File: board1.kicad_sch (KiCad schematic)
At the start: 24 parts, among them J1 Conn_01x14_Female, J2 Conn_01x05_Female, J3 Conn_01x14_Female, J4 Conn_01x20_Female, J5 Conn_01x20_Female, J6 XT30 Male Connector, U1 BNO085, U2 Teensy_4.0, U3 Raspberry_PI_Zero_W, U4 D24V50F5

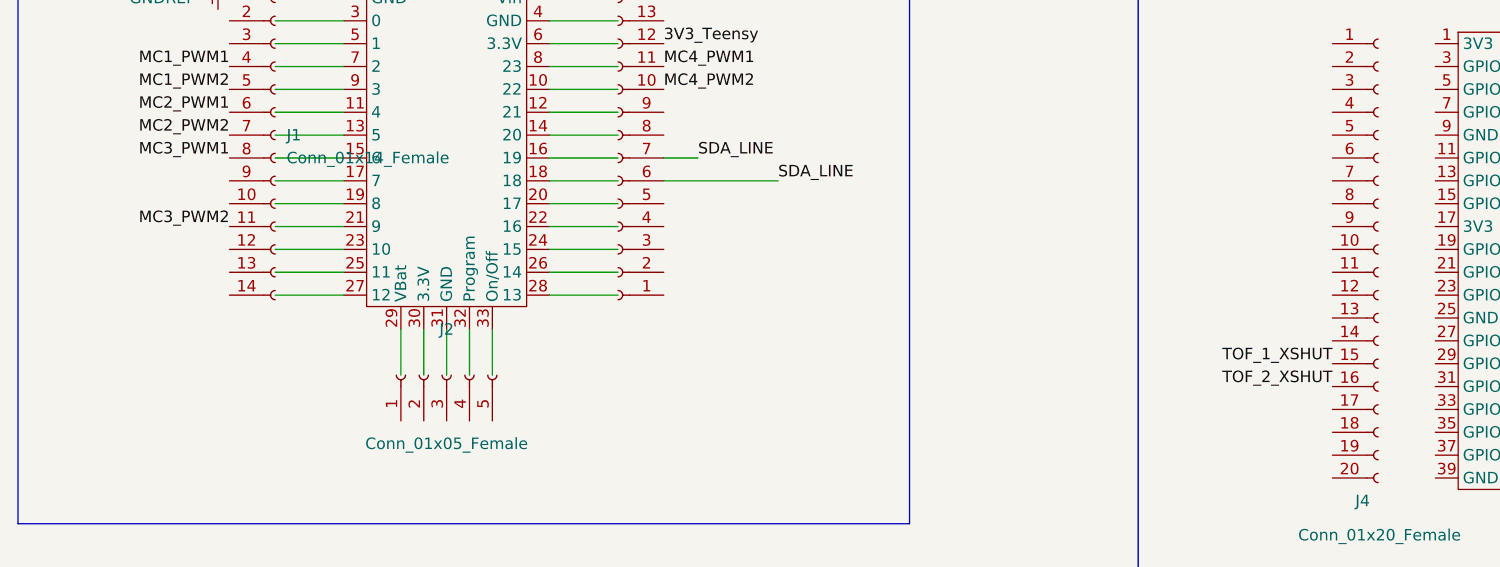
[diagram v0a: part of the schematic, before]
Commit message: Connected RPI to Teensy SPI
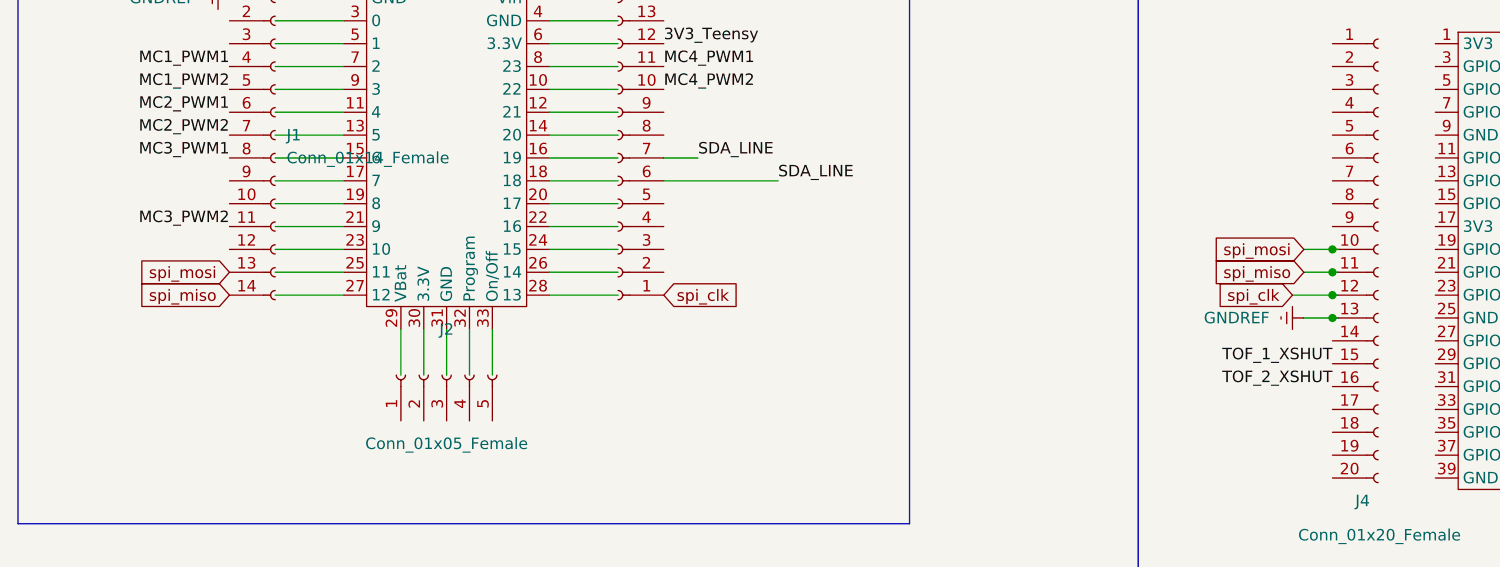
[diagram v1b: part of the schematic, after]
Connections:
- net GNDREF: now also J4.13 (Pin_13)
- net spi_mosi: now reaches J4.10 (Pin_10)
- net spi_mosi: now also J1.13 (Pin_13)
- net spi_miso: now reaches J4.11 (Pin_11)
- net spi_miso: now also J1.14 (Pin_14)
- net spi_clk: now reaches J4.12 (Pin_12)
- net spi_clk: now also J3.1 (Pin_1)
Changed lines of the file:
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@@
   (junction (at 113.665 223.52) (diameter 0) (color 0 0 0 0)
   )
+  (junction (at 173.355 78.74) (diameter 0) (color 0 0 0 0)
+  )
   (junction (at 158.115 227.33) (diameter 0) (color 0 0 0 0)
+  )
+  (junction (at 173.355 76.2) (diameter 0) (color 0 0 0 0)
+  )
+  (junction (at 173.355 73.66) (diameter 0) (color 0 0 0 0)
+  )
+  (junction (at 173.355 71.12) (diameter 0) (color 0 0 0 0)
   )
   (junction (at 120.65 223.52) (diameter 0) (color 0 0 0 0)
@@
     (stroke (width 0) (type default) (color 0 0 0 0))
   )
+  (wire (pts (xy 173.355 71.12) (xy 173.99 71.12))
+    (stroke (width 0) (type default) (color 0 0 0 0))
+  )
   (bus (pts (xy 126.365 149.225) (xy 27.305 149.225))
     (stroke (width 0) (type default) (color 0 0 0 0))
@@
     (stroke (width 0) (type default) (color 0 0 0 0))
   )
+  (wire (pts (xy 168.91 76.2) (xy 173.355 76.2))
+    (stroke (width 0) (type default) (color 0 0 0 0))
+  )
   (wire (pts (xy 86.36 66.04) (xy 93.98 66.04))
     (stroke (width 0) (type default) (color 0 0 0 0))
@@
     (stroke (width 0) (type default) (color 0 0 0 0))
   )
+  (wire (pts (xy 170.18 73.66) (xy 173.355 73.66))
+    (stroke (width 0) (type default) (color 0 0 0 0))
+  )
   (wire (pts (xy 55.88 66.04) (xy 63.5 66.04))
     (stroke (width 0) (type default) (color 0 0 0 0))
@@
     (stroke (width 0) (type default) (color 0 0 0 0))
   )
+  (wire (pts (xy 173.355 76.2) (xy 173.99 76.2))
+    (stroke (width 0) (type default) (color 0 0 0 0))
+  )
   (bus (pts (xy 260.985 157.48) (xy 260.985 267.97))
     (stroke (width 0) (type default) (color 0 0 0 0))
@@
     (stroke (width 0) (type default) (color 0 0 0 0))
   )
+  (wire (pts (xy 173.355 73.66) (xy 173.99 73.66))
+    (stroke (width 0) (type default) (color 0 0 0 0))
+  )
   (wire (pts (xy 207.645 212.09) (xy 212.725 212.09))
     (stroke (width 0) (type default) (color 0 0 0 0))
@@
     (stroke (width 0) (type default) (color 0 0 0 0))
   )
+  (wire (pts (xy 170.18 71.12) (xy 173.355 71.12))
+    (stroke (width 0) (type default) (color 0 0 0 0))
+  )
   (wire (pts (xy 158.115 203.2) (xy 173.355 203.2))
     (stroke (width 0) (type default) (color 0 0 0 0))
@@
     (stroke (width 0) (type default) (color 0 0 0 0))
   )
+  (wire (pts (xy 170.18 78.74) (xy 173.355 78.74))
+    (stroke (width 0) (type default) (color 0 0 0 0))
+  )
   (wire (pts (xy 72.39 80.01) (xy 72.39 85.09))
     (stroke (width 0) (type default) (color 0 0 0 0))
@@
   )
   (wire (pts (xy 86.36 68.58) (xy 93.98 68.58))
+    (stroke (width 0) (type default) (color 0 0 0 0))
+  )
+  (wire (pts (xy 173.355 78.74) (xy 173.99 78.74))
     (stroke (width 0) (type default) (color 0 0 0 0))
   )
@@
   (label "ENC_3_PINA" (at 302.26 232.41 0)
     (effects (font (size 1.27 1.27)) (justify left bottom))
+  )
+  (global_label "spi_mosi" (shape input) (at 50.8 73.66 180) (fields_autoplaced)
+    (effects (font (size 1.27 1.27)) (justify right))
+    (property "Intersheet References" "${INTERSHEET_REFS}" (id 0) (at 40.1621 73.5806 0)
+      (effects (font (size 1.27 1.27)) (justify right) hide)
+    )
+  )
+  (global_label "spi_miso" (shape input) (at 50.8 76.2 180) (fields_autoplaced)
+    (effects (font (size 1.27 1.27)) (justify right))
+    (property "Intersheet References" "${INTERSHEET_REFS}" (id 0) (at 40.1621 76.1206 0)
+      (effects (font (size 1.27 1.27)) (justify right) hide)
+    )
+  )
+  (global_label "spi_clk" (shape input) (at 168.91 76.2 180) (fields_autoplaced)
+    (effects (font (size 1.27 1.27)) (justify right))
+    (property "Intersheet References" "${INTERSHEET_REFS}" (id 0) (at 159.9655 76.1206 0)
+      (effects (font (size 1.27 1.27)) (justify right) hide)
+    )
+  )
+  (global_label "spi_clk" (shape input) (at 99.06 76.2 0) (fields_autoplaced)
+    (effects (font (size 1.27 1.27)) (justify left))
+    (property "Intersheet References" "${INTERSHEET_REFS}" (id 0) (at 108.0045 76.1206 0)
+      (effects (font (size 1.27 1.27)) (justify left) hide)
+    )
+  )
+  (global_label "spi_miso" (shape input) (at 170.18 73.66 180) (fields_autoplaced)
+    (effects (font (size 1.27 1.27)) (justify right))
+    (property "Intersheet References" "${INTERSHEET_REFS}" (id 0) (at 159.5421 73.5806 0)
+      (effects (font (size 1.27 1.27)) (justify right) hide)
+    )
+  )
+  (global_label "spi_mosi" (shape input) (at 170.18 71.12 180) (fields_autoplaced)
+    (effects (font (size 1.27 1.27)) (justify right))
+    (property "Intersheet References" "${INTERSHEET_REFS}" (id 0) (at 159.5421 71.0406 0)
+      (effects (font (size 1.27 1.27)) (justify right) hide)
+    )
   )
   (symbol (lib_id "Connector:Conn_01x20_Female") (at 178.435 71.12 0) (unit 1)
@@
     (pin "7")
     (pin "9")
+  )
+  (symbol (lib_id "power:GNDREF") (at 170.18 78.74 270) (unit 1)
+    (in_bom yes) (on_board yes) (fields_autoplaced)
+    (property "Reference" "#PWR?" (id 0) (at 163.83 78.74 0)
+      (effects (font (size 1.27 1.27)) hide)
+    )
+    (property "Value" "GNDREF" (id 1) (at 166.37 78.7399 90)
+      (effects (font (size 1.27 1.27)) (justify right))
+    )
+    (property "Footprint" "" (id 2) (at 170.18 78.74 0)
+      (effects (font (size 1.27 1.27)) hide)
+    )
+    (property "Datasheet" "" (id 3) (at 170.18 78.74 0)
+      (effects (font (size 1.27 1.27)) hide)
+    )
+    (pin "1")
   )
   (symbol (lib_id "board1_libs:DRV8876") (at 311.15 58.42 0) (unit 1)
@@
       (reference "#PWR0111") (unit 1) (value "GNDREF") (footprint "")
     )
+    (path "/35285334-a232-4009-8a88-5c715d42fa85"
+      (reference "#PWR?") (unit 1) (value "GNDREF") (footprint "")
+    )
     (path "/57e9e3a8-e7cd-4ce1-9637-24d055889e46"

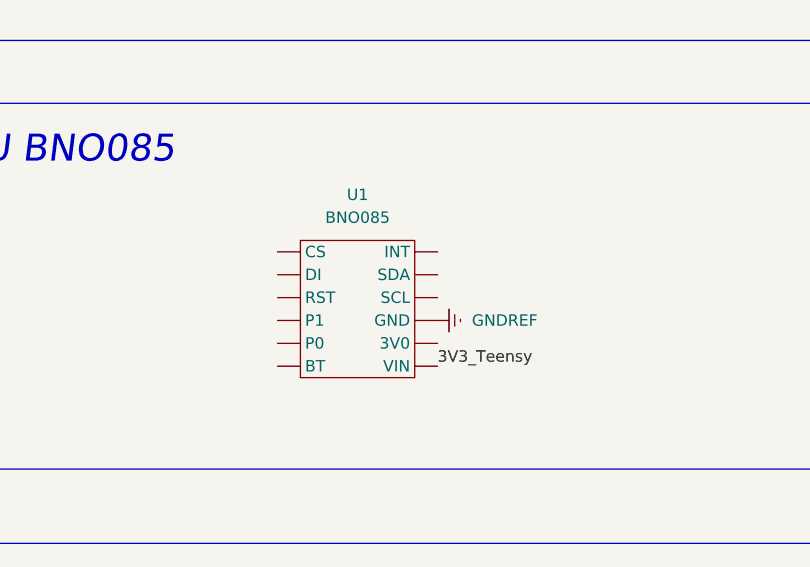
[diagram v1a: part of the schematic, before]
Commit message: Added SDA and SCL to IMU
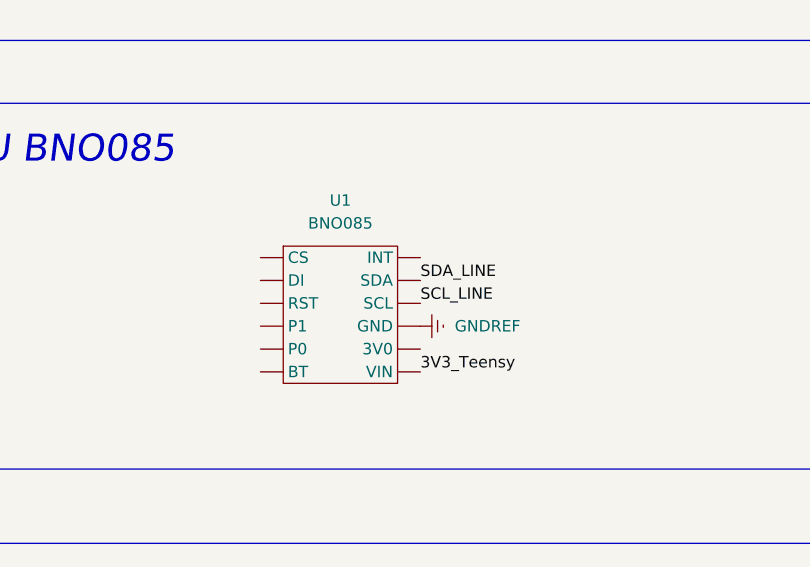
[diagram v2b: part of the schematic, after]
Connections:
- net SCL_LINE: now also U1. (VIN)
- net SDA_LINE: now also U1. (VIN)
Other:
- moved on the sheet: U1
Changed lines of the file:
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@@
     (effects (font (size 1.27 1.27)) (justify right bottom))
   )
-  (label "3V3_Teensy" (at 84.455 137.795 0)
+  (label "3V3_Teensy" (at 82.55 138.43 0)
     (effects (font (size 1.27 1.27)) (justify left bottom))
   )
@@
     (effects (font (size 1.27 1.27)) (justify left bottom))
   )
+  (label "SDA_LINE" (at 82.55 128.27 0)
+    (effects (font (size 1.27 1.27)) (justify left bottom))
+  )
   (label "MOTOR_4_PIN1" (at 335.28 237.49 0)
     (effects (font (size 1.27 1.27)) (justify left bottom))
@@
   )
   (label "TOF_3_XSHUT" (at 158.115 205.74 0)
+    (effects (font (size 1.27 1.27)) (justify left bottom))
+  )
+  (label "SCL_LINE" (at 82.55 130.81 0)
     (effects (font (size 1.27 1.27)) (justify left bottom))
   )
@@
     (pin "6")
   )
-  (symbol (lib_id "power:GNDREF") (at 84.455 132.715 90) (unit 1)
-    (in_bom yes) (on_board yes) (fields_autoplaced)
-    (property "Reference" "#PWR0104" (id 0) (at 90.805 132.715 0)
-      (effects (font (size 1.27 1.27)) hide)
-    )
-    (property "Value" "GNDREF" (id 1) (at 88.265 132.7149 90)
-      (effects (font (size 1.27 1.27)) (justify right))
-    )
-    (property "Footprint" "" (id 2) (at 84.455 132.715 0)
-      (effects (font (size 1.27 1.27)) hide)
-    )
-    (property "Datasheet" "" (id 3) (at 84.455 132.715 0)
+  (symbol (lib_id "power:GNDREF") (at 82.55 133.35 90) (unit 1)
+    (in_bom yes) (on_board yes) (fields_autoplaced)
+    (property "Reference" "#PWR0104" (id 0) (at 88.9 133.35 0)
+      (effects (font (size 1.27 1.27)) hide)
+    )
+    (property "Value" "GNDREF" (id 1) (at 86.36 133.3499 90)
+      (effects (font (size 1.27 1.27)) (justify right))
+    )
+    (property "Footprint" "" (id 2) (at 82.55 133.35 0)
+      (effects (font (size 1.27 1.27)) hide)
+    )
+    (property "Datasheet" "" (id 3) (at 82.55 133.35 0)
       (effects (font (size 1.27 1.27)) hide)
     )
@@
     (pin "9")
   )
-  (symbol (lib_id "board1_libs:BNO085") (at 75.565 122.555 0) (unit 1)
-    (in_bom yes) (on_board yes) (fields_autoplaced)
-    (property "Reference" "U1" (id 0) (at 75.565 118.745 0))
-    (property "Value" "BNO085" (id 1) (at 75.565 121.285 0))
-    (property "Footprint" "" (id 2) (at 75.565 122.555 0)
-      (effects (font (size 1.27 1.27)) hide)
-    )
-    (property "Datasheet" "" (id 3) (at 75.565 122.555 0)
-      (effects (font (size 1.27 1.27)) hide)
-    )
+  (symbol (lib_id "board1_libs:BNO085") (at 73.66 123.19 0) (unit 1)
+    (in_bom yes) (on_board yes) (fields_autoplaced)
+    (property "Reference" "U1" (id 0) (at 73.66 119.38 0))
+    (property "Value" "BNO085" (id 1) (at 73.66 121.92 0))
+    (property "Footprint" "" (id 2) (at 73.66 123.19 0)
+      (effects (font (size 1.27 1.27)) hide)
+    )
+    (property "Datasheet" "" (id 3) (at 73.66 123.19 0)
+      (effects (font (size 1.27 1.27)) hide)
+    )

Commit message: stuff
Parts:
- removed J1, J3: Conn_01x14_Female, symbol Connector:Conn_01x14_Female
- removed J2: Conn_01x05_Female, symbol Connector:Conn_01x05_Female
- removed J4, J5: Conn_01x20_Female, symbol Connector:Conn_01x20_Female
- removed TOF1, TOF2, TOF3, TOF4: VL53L4CXV0DH, LGA12_STM, symbol board1_libs:VL53L4CXV0DH/1
- added R3: 0 Ohms, board1_footprints:Resistor, symbol Device:R_US
- added TOF_STEMMA_QT1, TOF_STEMMA_QT2, TOF_STEMMA_QT3, TOF_STEMMA_QT4: Conn_01x04_Female, board1_footprints:Stemma QT, symbol Connector:Conn_01x04_Female
- added TOF_XSHUT1, TOF_XSHUT2, TOF_XSHUT3, TOF_XSHUT4: Conn_01x02_Female, Connector_PinSocket_2.54mm:PinSocket_1x02_P2.54mm_Vertical, symbol Connector:Conn_01x02_Female
- ENC_CONN1: footprint (none) -> Connector_PinHeader_2.54mm:PinHeader_1x06_P2.54mm_Vertical
- ENC_CONN2, ENC_CONN3, ENC_CONN4: footprint (none) -> Connector_PinSocket_2.54mm:PinSocket_1x06_P2.54mm_Vertical
- MC1, MC2, MC3, MC4: footprint (none) -> board1_footprints:DRV8876
- R1, R2: footprint (none) -> board1_footprints:Resistor
- U1: footprint (none) -> board1_footprints:BNU0085
- U2: footprint (none) -> board1_footprints:Teensy 4.0
- U3: footprint (none) -> Connector_PinHeader_2.54mm:PinHeader_2x20_P2.54mm_Vertical
- U4: footprint (none) -> board1_footprints:Voltage Regulator D24V50F5
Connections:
- net 12V: now also MC1.14 (VIN), MC2.14 (VIN), MC3.14 (VIN), MC4.14 (VIN); no longer MC1. (nSLEEP), MC2. (nSLEEP), MC3. (nSLEEP), MC4. (nSLEEP)
- net 3V3_Teensy: now also U1.7 (VIN), U2.6 (3.3V); no longer R1.2, R2.2, U1. (VIN)
- net 5V: now also MC1.5 (PMODE), MC1.6 (nSLEEP), MC2.5 (PMODE), MC2.6 (nSLEEP), MC3.5 (PMODE), MC3.6 (nSLEEP), MC4.5 (PMODE), MC4.6 (nSLEEP), U2.2 (Vin), U3.2 (5V); no longer MC1. (nSLEEP), MC2. (nSLEEP), MC3. (nSLEEP), MC4. (nSLEEP)
- net BATTERY_GROUND: now also MC1.13 (GND), MC2.13 (GND), MC3.13 (GND), MC4.13 (GND), R3.2; no longer MC1. (nSLEEP), MC2. (nSLEEP), MC3. (nSLEEP), MC4. (nSLEEP)
- net ENC_1_PINA: now also U2.12 (21)
- net ENC_1_PINB: now also U2.14 (20)
- net ENC_2_PINA: now also U2.16 (19)
- net ENC_2_PINB: now also U2.18
- net ENC_3_PINA: now also U2.20 (17)
- net ENC_3_PINB: now also U2.22 (16)
- net ENC_4_PINA: now also U2.24 (15)
- net ENC_4_PINB: now also U2.26 (14)
- net GNDREF: now also MC1.2 (GND), MC2.2 (GND), MC3.2 (GND), MC4.2 (GND), U1.9 (GND), U2.1 (GND), U3.25 (GND), U3.6 (GND), R3.1, TOF_STEMMA_QT1.1 (Pin_1), TOF_STEMMA_QT2.1 (Pin_1), TOF_STEMMA_QT3.1 (Pin_1), TOF_STEMMA_QT4.1 (Pin_1), TOF_XSHUT1.2 (Pin_2), TOF_XSHUT2.2 (Pin_2), TOF_XSHUT3.2 (Pin_2), TOF_XSHUT4.2 (Pin_2); no longer MC1. (nSLEEP), MC2. (nSLEEP), MC3. (nSLEEP), MC4. (nSLEEP), U1. (VIN)
- net MC1_PWM1: now also MC1.3 (EN/IN1), U2.7 (2); no longer MC1. (nSLEEP)
- net MC1_PWM2: now also MC1.4 (PH/IN2), U2.9 (3); no longer MC1. (nSLEEP)
- net MC2_PWM1: now also MC2.3 (EN/IN1), U2.11 (4); no longer MC2. (nSLEEP)
- net MC2_PWM2: now also MC2.4 (PH/IN2), U2.13 (5); no longer MC2. (nSLEEP)
- net MC3_PWM1: now also MC3.3 (EN/IN1), U2.15 (6); no longer MC3. (nSLEEP)
- net MC3_PWM2: now also MC3.4 (PH/IN2), U2.21 (9)
- net MC4_PWM1: now also MC4.3 (EN/IN1), U2.8 (23); no longer MC4. (nSLEEP)
- net MC4_PWM2: now also MC4.4 (PH/IN2), U2.10 (22)
- net MOTOR_1_PIN1: now also MC1.12 (OUT1); no longer MC1. (nSLEEP)
- net MOTOR_1_PIN2: now also MC1.11 (OUT2); no longer MC1. (nSLEEP)
- net MOTOR_2_PIN1: now also MC2.12 (OUT1); no longer MC2. (nSLEEP)
- net MOTOR_2_PIN2: now also MC2.11 (OUT2); no longer MC2. (nSLEEP)
- net MOTOR_3_PIN1: now also MC3.12 (OUT1); no longer MC3. (nSLEEP)
- net MOTOR_3_PIN2: now also MC3.11 (OUT2); no longer MC3. (nSLEEP)
- net MOTOR_4_PIN1: now also MC4.12 (OUT1); no longer MC4. (nSLEEP)
- net MOTOR_4_PIN2: now also MC4.11 (OUT2); no longer MC4. (nSLEEP)
- net SCL_LINE: now also U1.10 (SCL), U3.5 (GPIO_3_(SCL)), TOF_STEMMA_QT1.4 (Pin_4), TOF_STEMMA_QT2.4 (Pin_4), TOF_STEMMA_QT3.4 (Pin_4), TOF_STEMMA_QT4.4 (Pin_4); no longer U1. (VIN)
- net SDA_LINE: now also U1.11 (SDA), U3.3 (GPIO_2_(SDA)), TOF_STEMMA_QT1.3 (Pin_3), TOF_STEMMA_QT2.3 (Pin_3), TOF_STEMMA_QT3.3 (Pin_3), TOF_STEMMA_QT4.3 (Pin_3); no longer U1. (VIN)
- net TOF_1_XSHUT: now also U3.29 (GPIO_5), TOF_XSHUT1.1 (Pin_1)
- net TOF_2_XSHUT: now also U3.31 (GPIO_6), TOF_XSHUT2.1 (Pin_1)
- net TOF_3_XSHUT: now also U3.36 (GPIO_16), TOF_XSHUT3.1 (Pin_1)
- net TOF_4_XSHUT: now also U3.38 (GPIO_20), TOF_XSHUT4.1 (Pin_1)
- net UART TXD (R PI): now reaches U3.8 (GPIO_14_(TXD))
- net UART TXD (R PI): now also U2.3 (0)
- net UART RXD (R PI): now reaches U2.5 (1)
- net UART RXD (R PI): now also U3.10 (GPIO_15_(RXD))
- new net 3V3 RPI: R1.2, R2.2, TOF_STEMMA_QT1.2 (Pin_2), TOF_STEMMA_QT2.2 (Pin_2), TOF_STEMMA_QT3.2 (Pin_2), TOF_STEMMA_QT4.2 (Pin_2)
- no-connect marks 1 -> 66
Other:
- moved on the sheet: U3

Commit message: Updated Footprints
Updated Footprints to indicate physical limitations of components
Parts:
- U3: footprint Connector_PinHeader_2.54mm:PinHeader_2x20_P2.54mm_Vertical -> board1_footprints:Raspberry Pi Zero W
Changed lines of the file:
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@@
     (property "Reference" "U3" (id 0) (at 205.74 41.91 0))
     (property "Value" "Raspberry_PI_Zero_W" (id 1) (at 205.74 44.45 0))
-    (property "Footprint" "Connector_PinHeader_2.54mm:PinHeader_2x20_P2.54mm_Vertical" (id 2) (at 205.74 45.72 0)
+    (property "Footprint" "board1_footprints:Raspberry Pi Zero W" (id 2) (at 205.74 45.72 0)
       (effects (font (size 1.27 1.27)) hide)
     )
@@
     )
     (pin "1")
+    (pin "10")
     (pin "11")
     (pin "12")
@@
     (pin "7")
     (pin "8")
-    (pin "10")
     (pin "9")
   )
@@
     )
     (path "/82be1750-c848-4aaf-9b49-af208c0b90ce"
-      (reference "U3") (unit 1) (value "Raspberry_PI_Zero_W") (footprint "Connector_PinHeader_2.54mm:PinHeader_2x20_P2.54mm_Vertical")
+      (reference "U3") (unit 1) (value "Raspberry_PI_Zero_W") (footprint "board1_footprints:Raspberry Pi Zero W")
     )
     (path "/fea4ab70-5156-4f1c-9406-b94e14c07dcc"

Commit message: made changes
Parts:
- TOF_STEMMA_QT1, TOF_STEMMA_QT2, TOF_STEMMA_QT3, TOF_STEMMA_QT4: footprint board1_footprints:Stemma QT -> Connector_JST:JST_SH_BM04B-SRSS-TB_1x04-1MP_P1.00mm_Vertical
- U1: footprint board1_footprints:BNU0085 -> Connector_JST:JST_SH_BM04B-SRSS-TB_1x04-1MP_P1.00mm_Vertical
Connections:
- net 3V3 RPI is gone; now on net 3V3_Teensy: R1.2, R2.2, TOF_STEMMA_QT1.2 (Pin_2), TOF_STEMMA_QT2.2 (Pin_2), TOF_STEMMA_QT3.2 (Pin_2), TOF_STEMMA_QT4.2 (Pin_2)
- net 3V3_Teensy: now also MC1.6 (nSLEEP), MC2.6 (nSLEEP), MC3.6 (nSLEEP), MC4.6 (nSLEEP), U1.2 (VIN); no longer U1.7 (VIN)
- net 5V: no longer MC1.5 (PMODE), MC1.6 (nSLEEP), MC2.5 (PMODE), MC2.6 (nSLEEP), MC3.5 (PMODE), MC3.6 (nSLEEP), MC4.5 (PMODE), MC4.6 (nSLEEP)
- net ENC_1_PINA: now also U2.3 (0); no longer U2.12 (21)
- net ENC_1_PINB: now also U2.5 (1); no longer U2.14 (20)
- net ENC_2_PINA: now also U2.7 (2); no longer U2.16 (19)
- net ENC_2_PINB: now also U2.9 (3); no longer U2.18
- net ENC_3_PINA: now also U2.11 (4); no longer U2.20 (17)
- net ENC_3_PINB: now also U2.17 (7); no longer U2.22 (16)
- net ENC_4_PINA: now also U2.10 (22); no longer U2.24 (15)
- net ENC_4_PINB: now also U2.20 (17); no longer U2.26 (14)
- net GNDREF: now also MC1.5 (PMODE), MC2.5 (PMODE), MC3.5 (PMODE), MC4.5 (PMODE), U1.1 (GND); no longer U1.9 (GND), U3.25 (GND)
- net MC1_PWM1: now also U2.13 (5); no longer U2.7 (2)
- net MC1_PWM2: now also U2.15 (6); no longer U2.9 (3)
- net MC2_PWM1: now also U2.19 (8); no longer U2.11 (4)
- net MC2_PWM2: now also U2.21 (9); no longer U2.13 (5)
- net MC3_PWM1: now also U2.23 (10); no longer U2.15 (6)
- net MC3_PWM2: now also U2.25 (11); no longer U2.21 (9)
- net MC4_PWM1: now also U2.27 (12); no longer U2.8 (23)
- net MC4_PWM2: now also U2.8 (23); no longer U2.10 (22)
- net SCL_LINE: now also U1.4 (SCL), U2.16 (19); no longer U1.10 (SCL), U3.5 (GPIO_3_(SCL))
- net SDA_LINE: now also U1.3 (SDA), U2.18; no longer U1.11 (SDA), U3.3 (GPIO_2_(SDA))
- net TOF_1_XSHUT: now also U2.22 (16); no longer U3.29 (GPIO_5)
- net TOF_2_XSHUT: now also U2.24 (15); no longer U3.31 (GPIO_6)
- net TOF_3_XSHUT: now also U2.26 (14); no longer U3.36 (GPIO_16)
- net TOF_4_XSHUT: now also U2.28 (13); no longer U3.38 (GPIO_20)
- net UART RXD (R PI): now also U2.14 (20); no longer U2.5 (1)
- net UART TXD (R PI): now also U2.12 (21); no longer U2.3 (0)
- no-connect marks 66 -> 63
